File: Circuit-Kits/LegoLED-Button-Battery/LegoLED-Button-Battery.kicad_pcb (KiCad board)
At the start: 2 copper layers, 23.6 x 47.6 mm, 34 parts, among them SW1 Pushbutton

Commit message: Added v1.1 with protosnap but more clover-like boards.
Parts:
- removed the REF** at (160.0, 78.0)
- removed the REF** at (170.0, 88.0)
- removed the REF** at (160.0, 79.0)
- removed the REF** at (160.0, 80.0)
- removed the REF** at (160.0, 81.0)
- removed the REF** at (160.0, 82.0)
- removed the REF** at (167.0, 88.0)
- removed the REF** at (168.0, 88.0)
- removed the REF** at (169.0, 88.0)
- removed the REF** at (166.0, 88.0)
- added REF**: HOLE-UNPLATED-SNAP-1MM, Rewire_Circuits:HOLE-UNPLATED-SNAP-1MM, F.Cu at (168.0, 85.5)
- added REF**: HOLE-UNPLATED-SNAP-1MM, Rewire_Circuits:HOLE-UNPLATED-SNAP-1MM, F.Cu at (166.2, 87.7)
- added REF**: HOLE-UNPLATED-SNAP-1MM, Rewire_Circuits:HOLE-UNPLATED-SNAP-1MM, F.Cu at (170.0, 87.7)
- added REF**: HOLE-UNPLATED-SNAP-1MM, Rewire_Circuits:HOLE-UNPLATED-SNAP-1MM, F.Cu at (162.5, 80.0)
- added REF**: HOLE-UNPLATED-SNAP-1MM, Rewire_Circuits:HOLE-UNPLATED-SNAP-1MM, F.Cu at (160.3, 78.2)
- added REF**: HOLE-UNPLATED-SNAP-1MM, Rewire_Circuits:HOLE-UNPLATED-SNAP-1MM, F.Cu at (160.3, 82.0)
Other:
- outline, holes or cut-outs redrawn
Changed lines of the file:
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@@
     (area 104.572999 63.134905 187.431286 123.265001)
     (thickness 1.6)
-    (drawings 43)
+    (drawings 54)
     (tracks 45)
     (zones 0)
-    (modules 34)
+    (modules 30)
     (nets 4)
   )
@@
     (add_net "Net-(LED1-Pad+)")
   )
-  (module Rewire_Circuits:HOLE-UNPLATED-SNAP-0.5MM (layer F.Cu)
-    (at 160 78 90)
-    (fp_text reference REF** (at 0 0.5 90) (layer F.Fab) hide
-      (effects (font (size 1 1) (thickness 0.15)))
-    )
-    (fp_text value HOLE-UNPLATED-SNAP-0.5MM (at 0 -0.5 90) (layer F.Fab) hide
-      (effects (font (size 1 1) (thickness 0.15)))
-    )
-    (pad "" np_thru_hole circle (at 0 0 90) (size 0.5 0.5) (drill 0.5) (layers *.Cu))
-  )
-  (module Rewire_Circuits:HOLE-UNPLATED-SNAP-0.5MM (layer F.Cu)
-    (at 160 79 90)
-    (fp_text reference REF** (at 0 0.5 90) (layer F.Fab) hide
-      (effects (font (size 1 1) (thickness 0.15)))
-    )
-    (fp_text value HOLE-UNPLATED-SNAP-0.5MM (at 0 -0.5 90) (layer F.Fab) hide
-      (effects (font (size 1 1) (thickness 0.15)))
-    )
-    (pad "" np_thru_hole circle (at 0 0 90) (size 0.5 0.5) (drill 0.5) (layers *.Cu))
-  )
-  (module Rewire_Circuits:HOLE-UNPLATED-SNAP-0.5MM (layer F.Cu)
-    (at 160 80 90)
-    (fp_text reference REF** (at 0 0.5 90) (layer F.Fab) hide
-      (effects (font (size 1 1) (thickness 0.15)))
-    )
-    (fp_text value HOLE-UNPLATED-SNAP-0.5MM (at 0 -0.5 90) (layer F.Fab) hide
-      (effects (font (size 1 1) (thickness 0.15)))
-    )
-    (pad "" np_thru_hole circle (at 0 0 90) (size 0.5 0.5) (drill 0.5) (layers *.Cu))
-  )
-  (module Rewire_Circuits:HOLE-UNPLATED-SNAP-0.5MM (layer F.Cu)
-    (at 160 81 90)
-    (fp_text reference REF** (at 0 0.5 90) (layer F.Fab) hide
-      (effects (font (size 1 1) (thickness 0.15)))
-    )
-    (fp_text value HOLE-UNPLATED-SNAP-0.5MM (at 0 -0.5 90) (layer F.Fab) hide
-      (effects (font (size 1 1) (thickness 0.15)))
-    )
-    (pad "" np_thru_hole circle (at 0 0 90) (size 0.5 0.5) (drill 0.5) (layers *.Cu))
-  )
-  (module Rewire_Circuits:HOLE-UNPLATED-SNAP-0.5MM (layer F.Cu)
-    (at 160 82 90)
-    (fp_text reference REF** (at 0 0.5 90) (layer F.Fab) hide
-      (effects (font (size 1 1) (thickness 0.15)))
-    )
-    (fp_text value HOLE-UNPLATED-SNAP-0.5MM (at 0 -0.5 90) (layer F.Fab) hide
-      (effects (font (size 1 1) (thickness 0.15)))
-    )
-    (pad "" np_thru_hole circle (at 0 0 90) (size 0.5 0.5) (drill 0.5) (layers *.Cu))
-  )
-  (module Rewire_Circuits:HOLE-UNPLATED-SNAP-0.5MM (layer F.Cu)
-    (at 167 88 180)
-    (fp_text reference REF** (at 0 0.5 180) (layer F.Fab) hide
-      (effects (font (size 1 1) (thickness 0.15)))
-    )
-    (fp_text value HOLE-UNPLATED-SNAP-0.5MM (at 0 -0.5 180) (layer F.Fab) hide
-      (effects (font (size 1 1) (thickness 0.15)))
-    )
-    (pad "" np_thru_hole circle (at 0 0 180) (size 0.5 0.5) (drill 0.5) (layers *.Cu))
-  )
-  (module Rewire_Circuits:HOLE-UNPLATED-SNAP-0.5MM (layer F.Cu)
-    (at 168 88 180)
-    (fp_text reference REF** (at 0 0.5 180) (layer F.Fab) hide
-      (effects (font (size 1 1) (thickness 0.15)))
-    )
-    (fp_text value HOLE-UNPLATED-SNAP-0.5MM (at 0 -0.5 180) (layer F.Fab) hide
-      (effects (font (size 1 1) (thickness 0.15)))
-    )
-    (pad "" np_thru_hole circle (at 0 0 180) (size 0.5 0.5) (drill 0.5) (layers *.Cu))
-  )
-  (module Rewire_Circuits:HOLE-UNPLATED-SNAP-0.5MM (layer F.Cu)
-    (at 169 88 180)
-    (fp_text reference REF** (at 0 0.5 180) (layer F.Fab) hide
-      (effects (font (size 1 1) (thickness 0.15)))
-    )
-    (fp_text value HOLE-UNPLATED-SNAP-0.5MM (at 0 -0.5 180) (layer F.Fab) hide
-      (effects (font (size 1 1) (thickness 0.15)))
-    )
-    (pad "" np_thru_hole circle (at 0 0 180) (size 0.5 0.5) (drill 0.5) (layers *.Cu))
-  )
-  (module Rewire_Circuits:HOLE-UNPLATED-SNAP-0.5MM (layer F.Cu)
-    (at 166 88 180)
-    (fp_text reference REF** (at 0 0.5 180) (layer F.Fab) hide
-      (effects (font (size 1 1) (thickness 0.15)))
-    )
-    (fp_text value HOLE-UNPLATED-SNAP-0.5MM (at 0 -0.5 180) (layer F.Fab) hide
-      (effects (font (size 1 1) (thickness 0.15)))
-    )
-    (pad "" np_thru_hole circle (at 0 0 180) (size 0.5 0.5) (drill 0.5) (layers *.Cu))
-  )
-  (module Rewire_Circuits:HOLE-UNPLATED-SNAP-0.5MM (layer F.Cu)
-    (at 170 88 180)
-    (fp_text reference REF** (at 0 0.5 180) (layer F.Fab) hide
-      (effects (font (size 1 1) (thickness 0.15)))
-    )
-    (fp_text value HOLE-UNPLATED-SNAP-0.5MM (at 0 -0.5 180) (layer F.Fab) hide
-      (effects (font (size 1 1) (thickness 0.15)))
-    )
-    (pad "" np_thru_hole circle (at 0 0 180) (size 0.5 0.5) (drill 0.5) (layers *.Cu))
+  (module Rewire_Circuits:HOLE-UNPLATED-SNAP-1MM (layer F.Cu)
+    (at 167.98 85.5 270)
+    (fp_text reference REF** (at 0 0.5 270) (layer F.Fab) hide
+      (effects (font (size 1 1) (thickness 0.15)))
+    )
+    (fp_text value HOLE-UNPLATED-SNAP-1MM (at 0 -0.5 270) (layer F.Fab) hide
+      (effects (font (size 1 1) (thickness 0.15)))
+    )
+    (pad "" np_thru_hole circle (at 0 0 270) (size 1 1) (drill 1) (layers *.Cu))
+  )
+  (module Rewire_Circuits:HOLE-UNPLATED-SNAP-1MM (layer F.Cu)
+    (at 166.18 87.7)
+    (fp_text reference REF** (at 0 0.5) (layer F.Fab) hide
+      (effects (font (size 1 1) (thickness 0.15)))
+    )
+    (fp_text value HOLE-UNPLATED-SNAP-1MM (at 0 -0.5) (layer F.Fab) hide
+      (effects (font (size 1 1) (thickness 0.15)))
+    )
+    (pad "" np_thru_hole circle (at 0 0) (size 1 1) (drill 1) (layers *.Cu))
+  )
+  (module Rewire_Circuits:HOLE-UNPLATED-SNAP-1MM (layer F.Cu)
+    (at 169.98 87.7)
+    (fp_text reference REF** (at 0 0.5) (layer F.Fab) hide
+      (effects (font (size 1 1) (thickness 0.15)))
+    )
+    (fp_text value HOLE-UNPLATED-SNAP-1MM (at 0 -0.5) (layer F.Fab) hide
+      (effects (font (size 1 1) (thickness 0.15)))
+    )
+    (pad "" np_thru_hole circle (at 0 0) (size 1 1) (drill 1) (layers *.Cu))
+  )
+  (module Rewire_Circuits:HOLE-UNPLATED-SNAP-1MM (layer F.Cu)
+    (at 162.49 79.97 180)
+    (fp_text reference REF** (at 0 0.5 180) (layer F.Fab) hide
+      (effects (font (size 1 1) (thickness 0.15)))
+    )
+    (fp_text value HOLE-UNPLATED-SNAP-1MM (at 0 -0.5 180) (layer F.Fab) hide
+      (effects (font (size 1 1) (thickness 0.15)))
+    )
+    (pad "" np_thru_hole circle (at 0 0 180) (size 1 1) (drill 1) (layers *.Cu))
+  )
+  (module Rewire_Circuits:HOLE-UNPLATED-SNAP-1MM (layer F.Cu)
+    (at 160.29 78.17 270)
+    (fp_text reference REF** (at 0 0.5 270) (layer F.Fab) hide
+      (effects (font (size 1 1) (thickness 0.15)))
+    )
+    (fp_text value HOLE-UNPLATED-SNAP-1MM (at 0 -0.5 270) (layer F.Fab) hide
+      (effects (font (size 1 1) (thickness 0.15)))
+    )
+    (pad "" np_thru_hole circle (at 0 0 270) (size 1 1) (drill 1) (layers *.Cu))
+  )
+  (module Rewire_Circuits:HOLE-UNPLATED-SNAP-1MM (layer F.Cu)
+    (at 160.29 81.97 270)
+    (fp_text reference REF** (at 0 0.5 270) (layer F.Fab) hide
+      (effects (font (size 1 1) (thickness 0.15)))
+    )
+    (fp_text value HOLE-UNPLATED-SNAP-1MM (at 0 -0.5 270) (layer F.Fab) hide
+      (effects (font (size 1 1) (thickness 0.15)))
+    )
+    (pad "" np_thru_hole circle (at 0 0 270) (size 1 1) (drill 1) (layers *.Cu))
   )
   (module Rewire_Circuits:LED-5MMD-2.5MMP-2x2 (layer F.Cu)
@@
       (net 2 "Net-(BT1-Pad+)"))
   )
+  (gr_arc (start 172.348347 83.643186) (end 170.18 87.3) (angle 36.15760514) (layer Edge.Cuts) (width 0.1524))
+  (gr_arc (start 165.046085 84.984364) (end 167.471799 85.4) (angle 57.42107103) (layer Edge.Cuts) (width 0.1524))
+  (gr_arc (start 166.225607 87.699411) (end 166.225607 88.199411) (angle 153.4350001) (layer Edge.Cuts) (width 0.1524))
+  (gr_arc (start 167.98 85.5) (end 167.48 85.4) (angle 146.8886998) (layer Edge.Cuts) (width 0.1524))
+  (gr_arc (start 169.994305 87.735762) (end 170.18 87.3) (angle 159.1681201) (layer Edge.Cuts) (width 0.1524))
+  (gr_arc (start 160.254238 81.984305) (end 160.69 82.17) (angle 159.1681201) (layer Edge.Cuts) (width 0.1524))
+  (gr_arc (start 160.290589 78.215607) (end 159.790589 78.215607) (angle 153.4350001) (layer Edge.Cuts) (width 0.1524))
+  (gr_line (start 159.79 78.27) (end 159.79 81.97) (layer Edge.Cuts) (width 0.1524))
+  (gr_arc (start 162.49 79.97) (end 162.59 79.47) (angle 146.8886998) (layer Edge.Cuts) (width 0.1524))
+  (gr_arc (start 164.346814 84.338347) (end 160.69 82.17) (angle 36.15760514) (layer Edge.Cuts) (width 0.1524))
+  (gr_arc (start 163.005636 77.036085) (end 162.59 79.461799) (angle 57.42107103) (layer Edge.Cuts) (width 0.1524))
   (gr_line (start 158.3 88.2) (end 162 88.2) (layer Edge.Cuts) (width 0.1524))
   (gr_arc (start 164.368347 83.643186) (end 162.2 87.3) (angle 36.15760514) (layer Edge.Cuts) (width 0.1524))

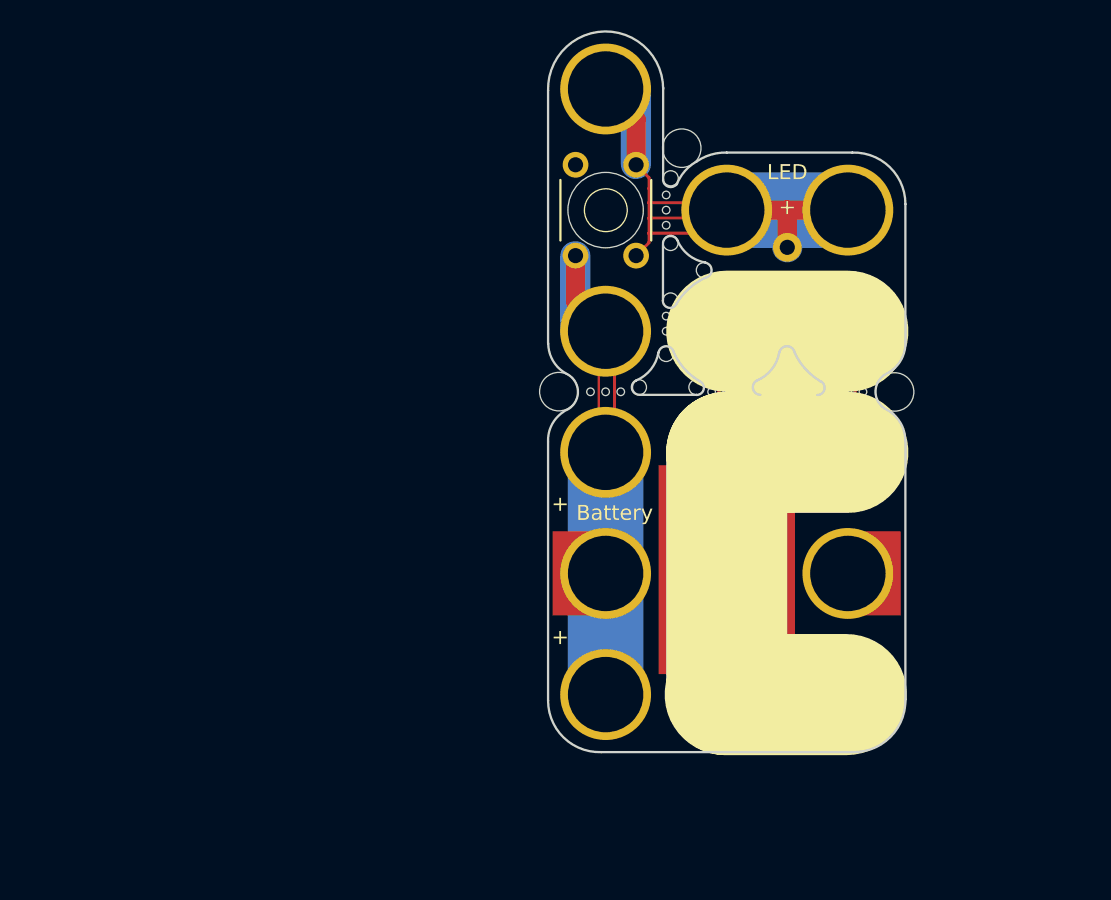
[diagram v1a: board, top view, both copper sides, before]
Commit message: Updated all library footprints.
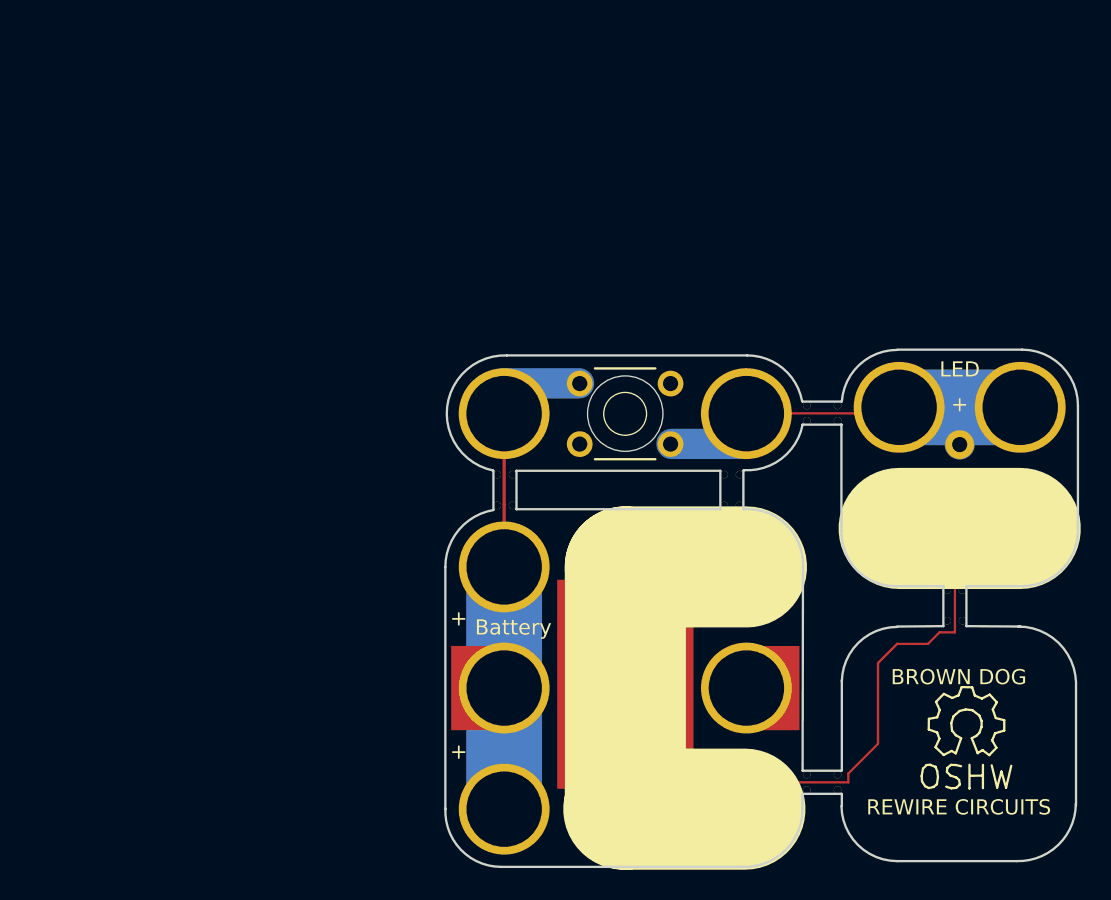
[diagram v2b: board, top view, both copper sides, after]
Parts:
- removed the REF** at (168.0, 85.5)
- removed the REF** at (175.1, 88.0)
- removed the REF** at (162.0, 87.7)
- removed the REF** at (163.0, 88.0)
- removed the REF** at (164.0, 88.0)
- removed the REF** at (173.0, 88.0)
- removed the REF** at (172.0, 88.0)
- removed the REF** at (171.0, 88.0)
- removed the REF** at (165.0, 88.0)
- removed the REF** at (160.0, 75.0)
- removed the REF** at (152.9, 88.0)
- removed the REF** at (166.2, 87.7)
- removed the REF** at (160.0, 84.0)
- removed the REF** at (160.0, 83.0)
- removed the REF** at (160.0, 76.0)
- removed the REF** at (160.0, 77.0)
- removed the REF** at (155.0, 88.0)
- removed the REF** at (157.0, 88.0)
- removed the REF** at (156.0, 88.0)
- removed the REF** at (158.2, 87.7)
- removed the REF** at (170.0, 87.7)
- removed the REF** at (162.5, 80.0)
- removed the REF** at (160.3, 78.2)
- removed the REF** at (160.3, 82.0)
- removed the REF** at (161.0, 71.9)
- removed the REF** at (160.0, 85.5)
- removed the REF** at (160.3, 73.9)
- added LOGO: BROWN DOG, Rewire_Circuits:LOGO-REWIRE-BDG-2x2, F.Cu at (179.3, 111.3)
- added REF**: SYMBOL-OSHW-LOGO-SILK, Wickerlib:SYMBOL-OSHW-LOGO-SILK, F.Cu at (179.8, 110.0)
- added REF**: TAB-20MIL-2x4-SNAP, Rewire_Circuits:TAB-20MIL-2x2-SNAP, F.Cu at (149.4, 94.5)
- added REF**: TAB-20MIL-2x4-SNAP, Rewire_Circuits:TAB-20MIL-2x2-SNAP, F.Cu at (164.3, 94.5)
- added REF**: TAB-20MIL-2x4-SNAP, Rewire_Circuits:TAB-20MIL-2x2-SNAP, F.Cu at (170.3, 113.8)
- added REF**: TAB-20MIL-2x4-SNAP, Rewire_Circuits:TAB-20MIL-2x2-SNAP, F.Cu at (179.1, 102.1)
- added REF**: TAB-20MIL-2x2-SNAP, Rewire_Circuits:TAB-20MIL-2x2-SNAP, F.Cu at (170.3, 89.4)
- moved LED1 17.8 mm to (183.4, 89.0)
- moved SW1 15.0 mm to (149.3, 89.4), turned to 0 degrees
- moved BT1 1.37 mm to (165.3, 99.6)
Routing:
- net Net-(LED1-Pad+): track 40.2 -> 10.3 mm
- net Net-(BT1-Pad+): track 22.7 -> 0.00 mm
- net (no net): track 0.00 -> 10.2 mm
- net GND: track 36.4 -> 42.0 mm
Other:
- board size 23.6 x 47.6 mm -> 41.8 x 34.2 mm
- board text added: "Assembly Information LegoLED-Button-Battery v1.3"
- board text added: "Rewire Circuit Kit 11/18/16"

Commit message: Tented the Lego holes on top side of CR2032 footprint.
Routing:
- net Net-(BT1-Pad+): track 0.00 -> 10.2 mm
- net (no net): track 10.2 -> 0.00 mm

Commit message: Update.
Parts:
- added BT1: Battery, Rewire_Circuits:CR2032-4x3-NO-ROTATE, F.Cu at (122.0, 107.0)
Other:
- board size 41.8 x 34.2 mm -> 69 x 34.2 mm
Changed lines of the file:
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@@
 (kicad_pcb (version 4) (host pcbnew 4.0.4+e1-6308~48~ubuntu16.04.1-stable)
   (general
-    (links 21)
+    (links 0)
     (no_connects 15)
     (area 104.572999 74.854999 190.697451 124.1552)
     (thickness 1.6)
-    (drawings 63)
+    (drawings 71)
     (tracks 25)
     (zones 0)
-    (modules 10)
+    (modules 11)
     (nets 4)
   )
@@
     (pad GND thru_hole circle (at 8 -8 180) (size 6 6) (drill 4.98) (layers *.Cu *.Mask)
       (net 1 GND))
-    (pad + thru_hole circle (at 0 -8 180) (size 6 6) (drill 4.98) (layers *.Cu B.Mask)
+    (pad + thru_hole circle (at 0 -8 180) (size 6 6) (drill 4.98) (layers *.Cu)
       (net 2 "Net-(BT1-Pad+)"))
     (pad + thru_hole circle (at 16 -8 180) (size 6 6) (drill 4.98) (layers *.Cu B.Mask)
@@
       (net 2 "Net-(BT1-Pad+)"))
   )
+  (module Rewire_Circuits:CR2032-4x3-NO-ROTATE (layer F.Cu)
+    (at 122 107)
+    (fp_text reference BT1 (at 4 -8 90) (layer F.Fab) hide
+      (effects (font (size 1 1) (thickness 0.15)))
+    )
+    (fp_text value Battery (at 15.4 -4) (layer F.SilkS)
+      (effects (font (size 1 1) (thickness 0.15)))
+    )
+    (fp_text user %R (at 8 -8) (layer F.Fab)
+      (effects (font (size 1 1) (thickness 0.15)))
+    )
+    (fp_line (start -3.8 -16) (end -3.8 8) (layer F.Fab) (width 0.05))
+    (fp_line (start 19.8 -16) (end 19.8 8) (layer F.Fab) (width 0.05))
+    (fp_line (start 0 -19.8) (end 16 -19.8) (layer F.Fab) (width 0.05))
+    (fp_arc (start 0 -16) (end -3.8 -16) (angle 90) (layer F.Fab) (width 0.05))
+    (fp_arc (start 16 -16) (end 16 -19.8) (angle 90) (layer F.Fab) (width 0.05))
+    (fp_line (start 0 0) (end 8 0) (layer B.SilkS) (width 8))
+    (fp_line (start 8 8) (end 8 -16) (layer F.SilkS) (width 8))
+    (fp_text user + (at 19 -3.4) (layer B.SilkS)
+      (effects (font (size 1 1) (thickness 0.15)) (justify mirror))
+    )
+    (fp_line (start 8 -16) (end 0 -16) (layer B.Mask) (width 5))
+    (fp_line (start 8 8) (end 8 -16) (layer B.Mask) (width 5))
+    (fp_line (start 0 0) (end 8 0) (layer B.Mask) (width 5))
+    (fp_line (start 8 -16) (end 8 8) (layer B.Cu) (width 5))
+    (fp_line (start 0 -16) (end 8 -16) (layer B.Cu) (width 5))
+    (fp_line (start 0 0) (end 8 0) (layer B.Cu) (width 5))
+    (fp_line (start 16 8) (end 16 -16) (layer B.Cu) (width 5))
+    (fp_text user + (at 19 -12.2) (layer F.SilkS)
+      (effects (font (size 1 1) (thickness 0.15)))
+    )
+    (fp_line (start 16 -16) (end 16 8) (layer B.Mask) (width 5))
+    (fp_line (start 0 -16) (end 8 -16) (layer B.SilkS) (width 8))
+    (fp_line (start 0 0) (end 0 8) (layer F.SilkS) (width 8))
+    (fp_text user + (at 19 -12.2) (layer B.SilkS)
+      (effects (font (size 1 1) (thickness 0.15)) (justify mirror))
+    )
+    (fp_text user + (at 19 -3.4) (layer F.SilkS)
+      (effects (font (size 1 1) (thickness 0.15)))
+    )
+    (fp_line (start 0.1 -16) (end 8.1 -16) (layer F.SilkS) (width 8))
+    (fp_line (start 0 8) (end 8 8) (layer F.SilkS) (width 8))
+    (fp_arc (start 16 8) (end 19.8 8) (angle 90) (layer F.Fab) (width 0.05))
+    (fp_arc (start 0 8) (end 0 11.8) (angle 90) (layer F.Fab) (width 0.05))
+    (fp_line (start 0 11.8) (end 16 11.8) (layer F.Fab) (width 0.05))
+    (fp_line (start 0 8) (end 8 8) (layer B.Cu) (width 5))
+    (fp_line (start 0 8) (end 8 8) (layer B.Mask) (width 5))
+    (fp_line (start 0 8) (end 8 8) (layer B.SilkS) (width 8))
+    (fp_line (start 0 0) (end 8 0) (layer F.SilkS) (width 8))
+    (fp_line (start 0 8) (end 0 0) (layer B.SilkS) (width 8))
+    (fp_line (start 8 8) (end 8 -16) (layer B.SilkS) (width 8))
+    (fp_line (start 0 8) (end 8 8) (layer B.Cu) (width 5))
+    (fp_line (start 0 8) (end 0 0) (layer B.Cu) (width 5))
+    (fp_line (start 0 8) (end 0 0) (layer B.Mask) (width 5))
+    (pad GND thru_hole circle (at 8 -8) (size 6 6) (drill 4.98) (layers *.Cu *.Mask))
+    (pad + thru_hole circle (at 0 -8) (size 6 6) (drill 4.98) (layers *.Cu))
+    (pad + thru_hole circle (at 16 -8) (size 6 6) (drill 4.98) (layers *.Cu B.Mask))
+    (pad + smd rect (at 18.2 -8) (size 2.6 5.56) (layers F.Cu F.Paste F.Mask))
+    (pad GND smd rect (at 7.996 -7.746) (size 9 13.8) (layers F.Cu F.Paste F.Mask))
+    (pad + smd rect (at -2.2 -8) (size 2.6 5.56) (layers F.Cu F.Paste F.Mask))
+    (pad GND thru_hole circle (at 0 -16) (size 6 6) (drill 4.98) (layers *.Cu *.Mask))
+    (pad GND thru_hole circle (at 8 -16) (size 6 6) (drill 4.98) (layers *.Cu *.Mask))
+    (pad + thru_hole circle (at 16 -16) (size 6 6) (drill 4.98) (layers *.Cu B.Mask))
+    (pad GND thru_hole circle (at 0 0) (size 6 6) (drill 4.98) (layers *.Cu *.Mask))
+    (pad GND thru_hole circle (at 8 0) (size 6 6) (drill 4.98) (layers *.Cu *.Mask))
+    (pad + thru_hole circle (at 16 0) (size 6 6) (drill 4.98) (layers *.Cu B.Mask))
+    (pad GND thru_hole circle (at 0 8) (size 6 6) (drill 4.98) (layers *.Cu *.Mask))
+    (pad GND thru_hole circle (at 8 8) (size 6 6) (drill 4.98) (layers *.Cu *.Mask))
+    (pad + thru_hole circle (at 16 8) (size 6 6) (drill 4.98) (layers *.Cu B.Mask))
+  )
+  (gr_arc (start 138 115) (end 141.8 115) (angle 90) (layer Edge.Cuts) (width 0.1524))
+  (gr_arc (start 122.093995 114.9) (end 122.093995 118.8) (angle 86.82016988) (layer Edge.Cuts) (width 0.1524))
+  (gr_line (start 122 118.8) (end 138 118.8) (layer Edge.Cuts) (width 0.1524))
+  (gr_arc (start 122 91) (end 118.2 91) (angle 90) (layer Edge.Cuts) (width 0.1524))
+  (gr_arc (start 137.906005 91.1) (end 137.906005 87.2) (angle 86.82016988) (layer Edge.Cuts) (width 0.1524))
+  (gr_line (start 141.8 90.9) (end 141.8 115) (layer Edge.Cuts) (width 0.1524))
+  (gr_line (start 118.2 91) (end 118.2 115.1) (layer Edge.Cuts) (width 0.1524))
+  (gr_line (start 138 87.2) (end 122 87.2) (layer Edge.Cuts) (width 0.1524))
   (gr_text "Rewire Circuit Kit\n11/18/16" (at 185.6232 122.428) (layer F.Fab)
     (effects (font (size 1.016 1.016) (thickness 0.1524)) (justify right))
